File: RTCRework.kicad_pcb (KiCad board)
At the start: 2 copper layers, 12 x 12 mm, 6 parts, among them J1 Conn_01x01, J2 Conn_01x01, U1 RT9058-33GV

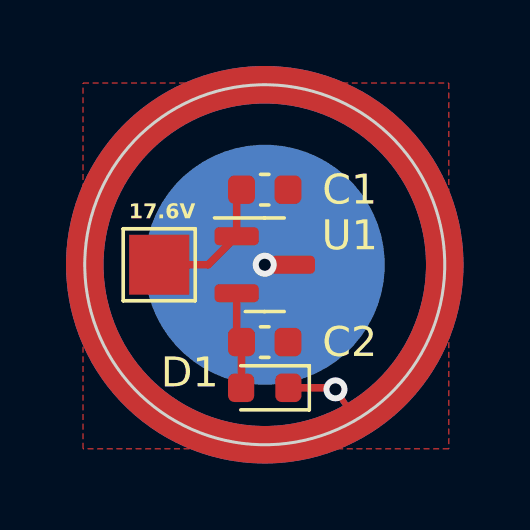
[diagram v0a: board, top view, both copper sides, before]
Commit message: Add fuse, switch to smaller packages
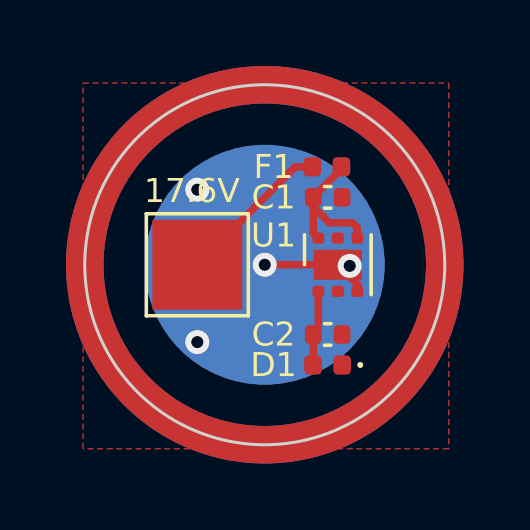
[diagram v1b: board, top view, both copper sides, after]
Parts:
- added F1: Fuse, Fuse:Fuse_0402_1005Metric, F.Cu at (52.1, 46.7)
- C1, C2: footprint Capacitor_SMD:C_0603_1608Metric -> Capacitor_SMD:C_0402_1005Metric
- D1: footprint Diode_SMD:D_0603_1608Metric -> Diode_SMD:D_0402_1005Metric
- J1: footprint TestPoint:TestPoint_Pad_2.0x2.0mm -> TestPoint:TestPoint_Pad_3.0x3.0mm
- U1: value RT9058-33GV -> NCP718AMT330TBG; footprint Package_TO_SOT_SMD:SOT-23 -> Package_SON:WSON-6-1EP_2x2mm_P0.65mm_EP1x1.6mm
- moved U1 2.44 mm to (52.4, 50.0), turned to 90 degrees
- moved D1 2.23 mm to (52.1, 53.3)
- moved C1 2.11 mm to (52.1, 47.8)
- moved C2 2.11 mm to (52.1, 52.3)
- moved J1 1.27 mm to (47.8, 50.0)
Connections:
- net /RTCBATT renamed +BATT
- C1 pad 1: /17.6VB -> Net-(U1-EN)
- J1 pad 1: /17.6VB -> +17.6V
- U1 pad 1: /17.6VB -> Net-(D1-A)
- U1 pad 2: Net-(D1-A) -> unconnected-(U1-NC-Pad2)
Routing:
- net Net-(U1-EN): track 0.00 -> 5.25 mm
- net +17.6V: track 0.00 -> 5.18 mm
- net /17.6VB: track 4.59 -> 0.00 mm
- net GND: track 0.94 -> 3.80 mm, vias 1 -> 4
- net +BATT: track 1.59 -> 0.00 mm, vias 1 -> 0
- net Net-(D1-A): track 3.22 -> 2.53 mm

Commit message: Update dimensions
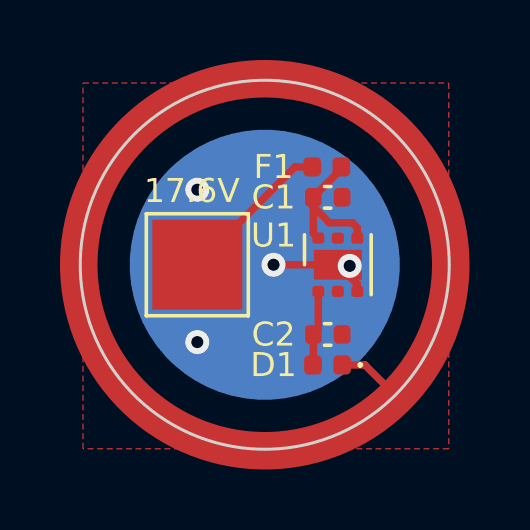
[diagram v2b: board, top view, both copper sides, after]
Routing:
- net +BATT: track 0.00 -> 1.84 mm
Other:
- board size 12 x 12 mm -> 12.3 x 12.3 mm
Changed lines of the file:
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@@
         (effects (font (size 1 1) (thickness 0.15)) (justify mirror))
     )
-    (fp_circle (center 0 0) (end 4.5 0)
+    (fp_circle (center 0 0) (end 4.75 0)
       (stroke (width 0.12) (type solid)) (fill none) (layer "B.SilkS"))
     (fp_circle (center 0 0) (end 5 0)
       (stroke (width 0.05) (type solid)) (fill none) (layer "B.CrtYd"))
-    (pad "1" smd circle (at 0 0 180) (size 8 8) (layers "B.Cu" "B.Mask")
+    (pad "1" smd circle (at 0 0 180) (size 9 9) (layers "B.Cu" "B.Mask")
       (net 2 "GND") (pinfunction "Pin_1") (pintype "passive"))
   )
-  (gr_circle (center 50 50) (end 56 50)
+  (gr_circle (center 50 50) (end 56.2 50)
     (stroke (width 1.25) (type solid)) (fill none) (layer "F.Cu"))
-  (gr_circle (center 50 50) (end 56 50)
-    (stroke (width 1.25) (type solid)) (fill none) (layer "B.Cu"))
-  (gr_circle (center 50 50) (end 56 50)
-    (stroke (width 1.3) (type solid)) (fill none) (layer "B.Mask"))
-  (gr_circle (center 50 50) (end 56 50)
+  (gr_circle (center 50 50) (end 56.2 50)
+    (stroke (width 0.2) (type solid)) (fill none) (layer "B.Cu"))
+  (gr_circle (center 50 50) (end 56.2 50)
+    (stroke (width 0.2) (type solid)) (fill none) (layer "B.Mask"))
+  (gr_circle (center 50 50) (end 56.2 50)
     (stroke (width 1.3) (type solid)) (fill none) (layer "F.Mask"))
-  (gr_circle (center 50 50) (end 56 50)
+  (gr_circle (center 50 50) (end 56.15 50)
     (stroke (width 0.1) (type default)) (fill none) (layer "Edge.Cuts"))
   (gr_text "17.6V" (at 45.974 48.006) (layer "F.SilkS")
     (effects (font (size 0.8 0.8) (thickness 0.12)) (justify left bottom))
   )
+  (segment (start 53.34 53.34) (end 54.102 54.102) (width 0.25) (layer "F.Cu") (net 1))
+  (segment (start 52.578 53.34) (end 53.34 53.34) (width 0.25) (layer "F.Cu") (net 1))
   (segment (start 52.832 50.038) (end 52.474 50.038) (width 0.25) (layer "F.Cu") (net 2))
   (segment (start 53.086 50.8875) (end 53.086 50.65) (width 0.25) (layer "F.Cu") (net 2))
   (segment (start 53.086 50.65) (end 52.832 50.396) (width 0.25) (layer "F.Cu") (net 2))
-  (segment (start 52.436 50) (end 50 50) (width 0.25) (layer "F.Cu") (net 2))
   (segment (start 52.832 50.396) (end 52.832 50.038) (width 0.25) (layer "F.Cu") (net 2))
+  (segment (start 52.436 50) (end 50.292 50) (width 0.25) (layer "F.Cu") (net 2))
   (segment (start 52.474 50.038) (end 52.436 50) (width 0.25) (layer "F.Cu") (net 2))
-  (via (at 50 50) (size 0.8) (drill 0.4) (layers "F.Cu" "B.Cu") (net 2))
+  (via (at 50.292 50) (size 0.8) (drill 0.4) (layers "F.Cu" "B.Cu") (net 2))
   (via (at 47.752 47.498) (size 0.8) (drill 0.4) (layers "F.Cu" "B.Cu") (net 2))
   (via (at 47.752 52.578) (size 0.8) (drill 0.4) (layers "F.Cu" "B.Cu") (net 2))
